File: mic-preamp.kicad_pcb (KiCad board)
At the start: 2 copper layers, 11 parts, among them J1 Conn_01x07_Female, J2 Conn_01x04_Female, U1 LM358

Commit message: gg
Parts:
- moved R1 9.58 mm to (145.6, 104.9)
- moved C2 5.22 mm to (161.5, 100.2), turned to 0 degrees
- moved R3 3.97 mm to (165.1, 110.5), turned to 90 degrees
- moved R2 2.78 mm to (166.2, 110.7)
- moved U1 1.47 mm to (154.3, 103.6)
- moved C3 1.33 mm to (152.8, 114.4)
- moved R4 1.20 mm to (152.5, 100.1)
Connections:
- J1 pad 2: Net-(J1-Pad2) -> (no net)
- J1 pad 3: FREQUPDN -> (no net)
- J1 pad 4: Net-(J1-Pad4) -> (no net)
- J2 pad 2: MICOUT -> PTT
- J2 pad 3: PTT -> MICGND
- J2 pad 4: MICGND -> MICOUT
- U1 pad 1: MICOUT -> (no net)
- U1 pad 2: Net-(C3-Pad2) -> (no net)
- U1 pad 3: +2V5 -> (no net)
- U1 pad 5: (no net) -> +2V5
- U1 pad 6: (no net) -> Net-(C3-Pad2)
- U1 pad 7: (no net) -> MICOUT
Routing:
- net PTT: track 0.00 -> 56.2 mm
- net +2V5: track 3.55 -> 32.0 mm
- net MICOUT: track 53.4 -> 26.3 mm
- net +5V: track 18.2 -> 41.4 mm
- net MICIN: track 6.13 -> 21.7 mm
- net Net-(C1-Pad2): track 5.51 -> 6.72 mm
- net Net-(C3-Pad2): track 19.3 -> 18.4 mm
- net MICGND: vias 0 -> 2
- added copper zone on B.Cu, net MICGND
- added copper zone on F.Cu, net MICGND
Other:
- board outline added: 42.5 x 23.7 mm

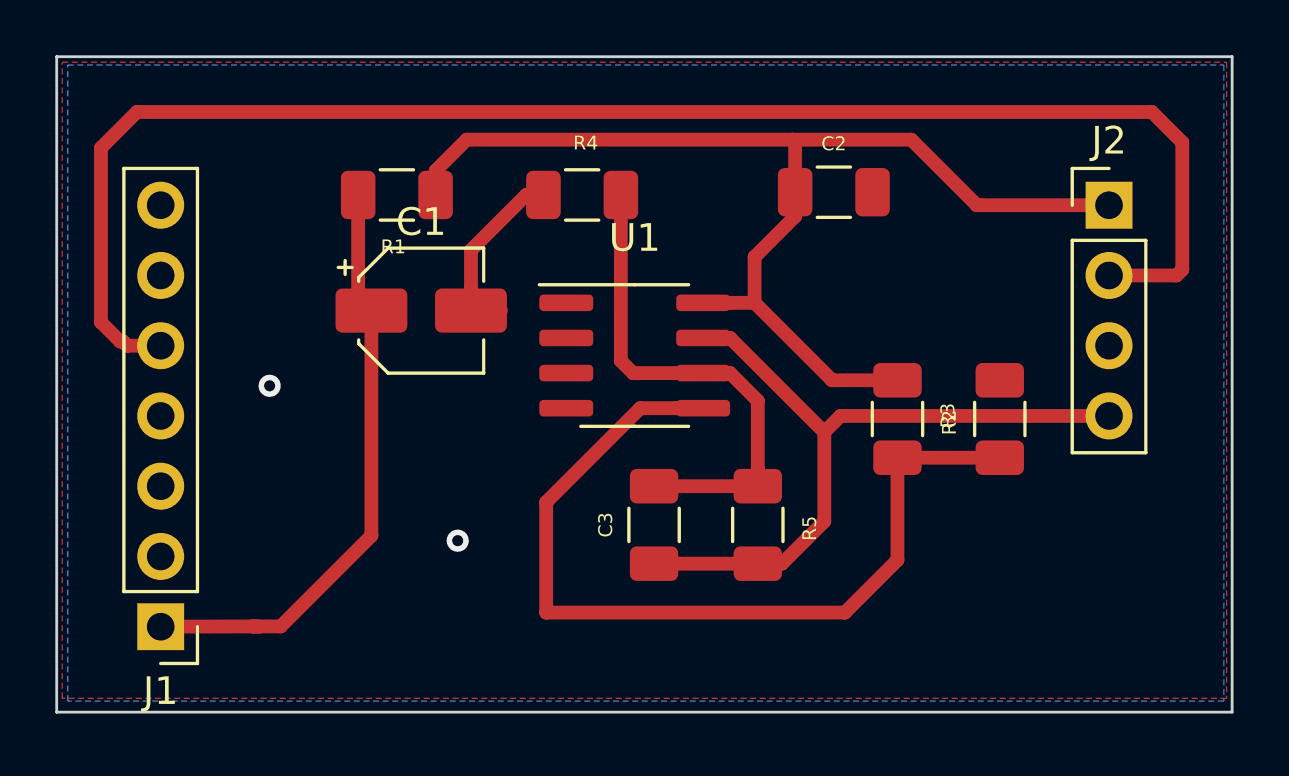
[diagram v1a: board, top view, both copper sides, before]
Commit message: added output cap
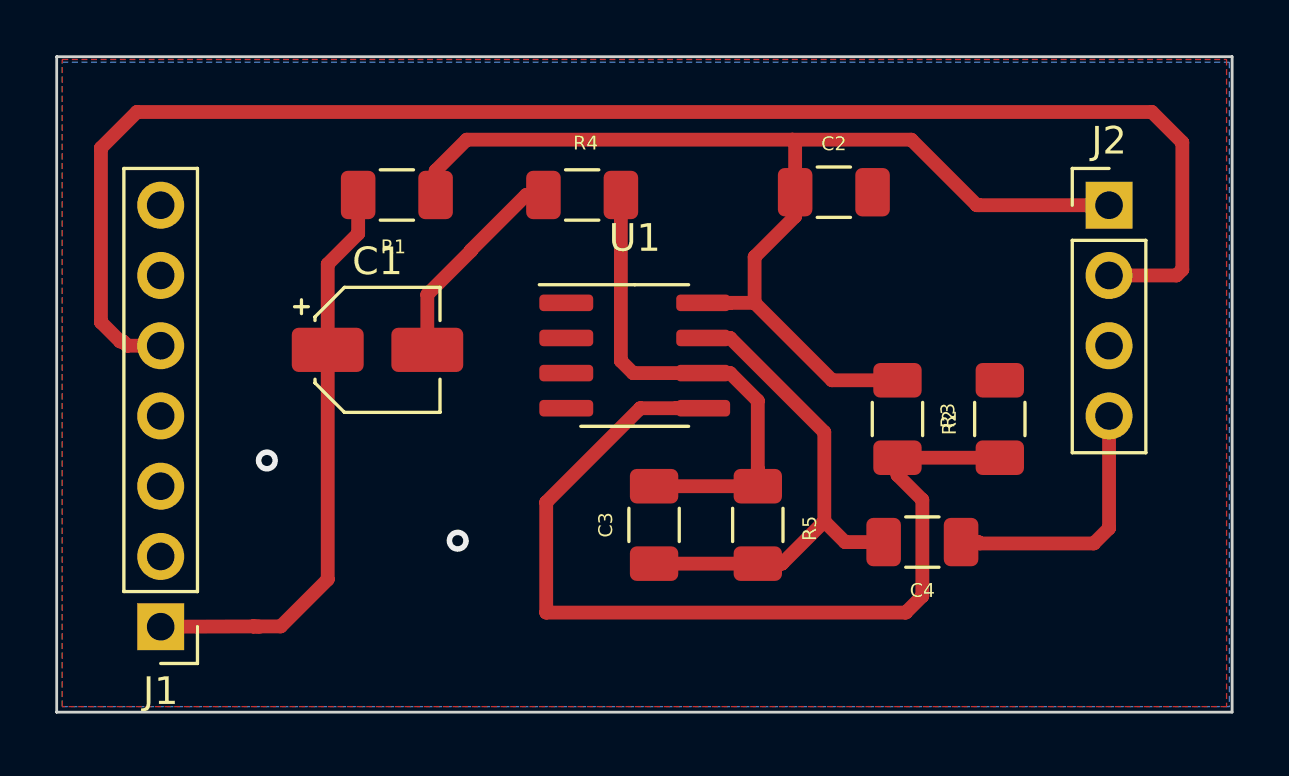
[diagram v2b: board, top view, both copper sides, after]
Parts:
- added C4: 100nF, Xenir:Capacitor 1206, F.Cu at (164.7, 117.3)
- moved C1 2.12 mm to (145.0, 108.1)
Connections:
- C3 pad 1: MICOUT -> Net-(C3-Pad1)
- R5 pad 2: MICOUT -> Net-(C3-Pad1)
- U1 pad 7: MICOUT -> Net-(C3-Pad1)
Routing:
- net Net-(C3-Pad1): track 0.00 -> 18.3 mm
- net MICOUT: track 26.3 -> 9.66 mm
- net +2V5: track 32.0 -> 34.0 mm
- net Net-(C1-Pad2): track 6.72 -> 7.71 mm
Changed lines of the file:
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@@
     (thickness 1.6)
     (drawings 4)
-    (tracks 65)
+    (tracks 73)
     (zones 0)
-    (modules 11)
-    (nets 9)
+    (modules 12)
+    (nets 10)
   )
   (page A4)
@@
   (net 7 PTT)
   (net 8 +2V5)
+  (net 9 "Net-(C3-Pad1)")
   (net_class Default "This is the default net class."
     (clearance 0.2)
@@
     (add_net MICOUT)
     (add_net "Net-(C1-Pad2)")
+    (add_net "Net-(C3-Pad1)")
     (add_net "Net-(C3-Pad2)")
     (add_net PTT)
+  )
+  (module "Xenir:Capacitor 1206" (layer F.Cu)
+    (at 164.7 117.3 180)
+    (fp_text reference C4 (at 0 0.5) (layer F.SilkS)
+      (effects (font (size 0.5 0.5) (thickness 0.125)))
+    )
+    (fp_text value 100nF (at 0.5 4) (layer F.Fab)
+      (effects (font (size 0.5 0.5) (thickness 0.125)))
+    )
+    (fp_text user %R (at 0 2.25) (layer F.Fab)
+      (effects (font (size 0.8 0.8) (thickness 0.12)))
+    )
+    (fp_line (start -1.6 3.05) (end -1.6 1.45) (layer F.Fab) (width 0.1))
+    (fp_line (start 2.28 1.13) (end 2.28 3.37) (layer F.CrtYd) (width 0.05))
+    (fp_line (start -1.6 1.45) (end 1.6 1.45) (layer F.Fab) (width 0.1))
+    (fp_line (start -2.28 3.37) (end -2.28 1.13) (layer F.CrtYd) (width 0.05))
+    (fp_line (start -0.602064 1.34) (end 0.602064 1.34) (layer F.SilkS) (width 0.12))
+    (fp_line (start -0.602064 3.16) (end 0.602064 3.16) (layer F.SilkS) (width 0.12))
+    (fp_line (start -2.28 1.13) (end 2.28 1.13) (layer F.CrtYd) (width 0.05))
+    (fp_line (start 2.28 3.37) (end -2.28 3.37) (layer F.CrtYd) (width 0.05))
+    (fp_line (start 1.6 3.05) (end -1.6 3.05) (layer F.Fab) (width 0.1))
+    (fp_line (start 1.6 1.45) (end 1.6 3.05) (layer F.Fab) (width 0.1))
+    (pad 2 smd roundrect (at 1.4 2.25 180) (size 1.25 1.75) (layers F.Cu F.Paste F.Mask) (roundrect_rratio 0.2)
+      (net 9 "Net-(C3-Pad1)"))
+    (pad 1 smd roundrect (at -1.4 2.25 180) (size 1.25 1.75) (layers F.Cu F.Paste F.Mask) (roundrect_rratio 0.2)
+      (net 6 MICOUT))
   )
   (module "Xenir:Resistor 1206" (layer F.Cu)
@@
     (pad 3 smd roundrect (at -2.475 5.385) (size 1.95 0.6) (layers F.Cu F.Paste F.Mask) (roundrect_rratio 0.25))
     (pad 7 smd roundrect (at 2.475 4.115) (size 1.95 0.6) (layers F.Cu F.Paste F.Mask) (roundrect_rratio 0.25)
-      (net 6 MICOUT))
+      (net 9 "Net-(C3-Pad1)"))
     (pad 5 smd roundrect (at 2.475 6.655) (size 1.95 0.6) (layers F.Cu F.Paste F.Mask) (roundrect_rratio 0.25)
       (net 8 +2V5))
@@
     (fp_line (start -2.407 3.497) (end -2.407 1.257) (layer F.CrtYd) (width 0.05))
     (pad 2 smd roundrect (at 1.273 2.377 270) (size 1.25 1.75) (layers F.Cu F.Paste F.Mask) (roundrect_rratio 0.2)
-      (net 6 MICOUT))
+      (net 9 "Net-(C3-Pad1)"))
     (pad 1 smd roundrect (at -1.527 2.377 270) (size 1.25 1.75) (layers F.Cu F.Paste F.Mask) (roundrect_rratio 0.2)
       (net 5 "Net-(C3-Pad2)"))
@@
       (net 5 "Net-(C3-Pad2)"))
     (pad 1 smd roundrect (at -1.4 2.25 90) (size 1.25 1.75) (layers F.Cu F.Paste F.Mask) (roundrect_rratio 0.2)
-      (net 6 MICOUT))
+      (net 9 "Net-(C3-Pad1)"))
   )
   (module "Xenir:Capacitor 1206" (layer F.Cu)
@@
   )
   (module Capacitor_SMD:CP_Elec_4x5.4 (layer F.Cu)
-    (at 146.58 106.68)
+    (at 145 108.1)
     (descr "SMD capacitor, aluminum electrolytic, Panasonic A5 / Nichicon, 4.0x5.4mm")
     (tags "capacitor electrolytic")
@@
   (gr_line (start 133.4 121.2) (end 133.4 97.5) (layer Edge.Cuts) (width 0.1))
   (gr_line (start 175.9 121.2) (end 133.4 121.2) (layer Edge.Cuts) (width 0.1))
-  (segment (start 149.465 106.68) (end 148.38 106.68) (width 0.5) (layer F.Cu) (net 1))
-  (segment (start 148.38 105.88) (end 148.38 106.68) (width 0.5) (layer F.Cu) (net 1))
+  (segment (start 146.8 106.1) (end 146.8 108.1) (width 0.5) (layer F.Cu) (net 1))
+  (segment (start 148.38 104.52) (end 146.8 106.1) (width 0.5) (layer F.Cu) (net 1))
+  (segment (start 148.38 104.495) (end 148.38 104.52) (width 0.5) (layer F.Cu) (net 1))
+  (segment (start 151 102.5) (end 150.375 102.5) (width 0.5) (layer F.Cu) (net 1))
   (segment (start 150.375 102.5) (end 148.38 104.495) (width 0.5) (layer F.Cu) (net 1))
-  (segment (start 148.38 104.495) (end 148.38 105.88) (width 0.5) (layer F.Cu) (net 1))
-  (segment (start 151 102.5) (end 150.375 102.5) (width 0.5) (layer F.Cu) (net 1))
-  (segment (start 144.3 106.2) (end 144.78 106.68) (width 0.5) (layer F.Cu) (net 2))
-  (segment (start 144.3 102.5) (end 144.3 106.2) (width 0.5) (layer F.Cu) (net 2))
-  (segment (start 144.78 106.68) (end 144.78 114.82) (width 0.5) (layer F.Cu) (net 2))
   (segment (start 141.5 118.1) (end 140.5 118.1) (width 0.5) (layer F.Cu) (net 2))
-  (segment (start 144.78 114.82) (end 141.5 118.1) (width 0.5) (layer F.Cu) (net 2))
   (segment (start 137.16 118.11) (end 140.5 118.1) (width 0.5) (layer F.Cu) (net 2))
   (segment (start 140.5 118.1) (end 140.735 118.11) (width 0.5) (layer F.Cu) (net 2))
-  (via (at 141.1 109.4) (size 0.8) (drill 0.4) (layers F.Cu B.Cu) (net 3))
+  (segment (start 144.3 102.5) (end 144.3 103.9) (width 0.5) (layer F.Cu) (net 2))
+  (segment (start 143.2 105) (end 143.2 108.1) (width 0.5) (layer F.Cu) (net 2))
+  (segment (start 144.3 103.9) (end 143.2 105) (width 0.5) (layer F.Cu) (net 2))
+  (segment (start 143.2 116.4) (end 141.5 118.1) (width 0.5) (layer F.Cu) (net 2))
+  (segment (start 143.2 108.1) (end 143.2 116.4) (width 0.5) (layer F.Cu) (net 2))
+  (via (at 141 112.1) (size 0.8) (drill 0.4) (layers F.Cu B.Cu) (net 3))
   (via (at 147.9 115) (size 0.8) (drill 0.4) (layers F.Cu B.Cu) (net 3))
   (segment (start 171.45 102.87) (end 166.755 102.87) (width 0.5) (layer F.Cu) (net 4))
@@
   (segment (start 153.8 108.5) (end 154.24 108.94) (width 0.5) (layer F.Cu) (net 5))
   (segment (start 158.75 113.03) (end 155 113.03) (width 0.5) (layer F.Cu) (net 5))
-  (segment (start 161.155 111.075) (end 161.155 114.3) (width 0.5) (layer F.Cu) (net 6))
-  (segment (start 159.625 115.83) (end 158.75 115.83) (width 0.5) (layer F.Cu) (net 6))
-  (segment (start 161.155 114.3) (end 159.625 115.83) (width 0.5) (layer F.Cu) (net 6))
-  (segment (start 157.75 107.67) (end 161.155 111.075) (width 0.5) (layer F.Cu) (net 6))
-  (segment (start 156.775 107.67) (end 157.75 107.67) (width 0.5) (layer F.Cu) (net 6))
-  (segment (start 161.74 110.49) (end 171.45 110.49) (width 0.5) (layer F.Cu) (net 6))
-  (segment (start 161.155 111.075) (end 161.74 110.49) (width 0.5) (layer F.Cu) (net 6))
-  (segment (start 158.75 115.83) (end 155 115.83) (width 0.5) (layer F.Cu) (net 6))
+  (segment (start 166.725 115.05) (end 166.775 115.1) (width 0.5) (layer F.Cu) (net 6))
+  (segment (start 166.1 115.05) (end 166.725 115.05) (width 0.5) (layer F.Cu) (net 6))
+  (segment (start 166.775 115.1) (end 170.9 115.1) (width 0.5) (layer F.Cu) (net 6))
+  (segment (start 171.45 114.55) (end 171.45 110.49) (width 0.5) (layer F.Cu) (net 6))
+  (segment (start 170.9 115.1) (end 171.45 114.55) (width 0.5) (layer F.Cu) (net 6))
+  (segment (start 161.155 111.075) (end 161.155 114.3) (width 0.5) (layer F.Cu) (net 9))
+  (segment (start 159.625 115.83) (end 158.75 115.83) (width 0.5) (layer F.Cu) (net 9))
+  (segment (start 161.155 114.3) (end 159.625 115.83) (width 0.5) (layer F.Cu) (net 9))
+  (segment (start 157.75 107.67) (end 161.155 111.075) (width 0.5) (layer F.Cu) (net 9))
+  (segment (start 156.775 107.67) (end 157.75 107.67) (width 0.5) (layer F.Cu) (net 9))
+  (segment (start 158.75 115.83) (end 155 115.83) (width 0.5) (layer F.Cu) (net 9))
   (segment (start 174.1 105.2) (end 173.89 105.41) (width 0.5) (layer F.Cu) (net 7))
   (segment (start 173 99.5) (end 174.1 100.6) (width 0.5) (layer F.Cu) (net 7))
@@
   (segment (start 135.7 107.8) (end 135 107.1) (width 0.5) (layer F.Cu) (net 7))
   (segment (start 167.5 112) (end 163.8 112) (width 0.5) (layer F.Cu) (net 8))
-  (segment (start 155.8 110.21) (end 156.775 110.21) (width 0.5) (layer F.Cu) (net 8))
-  (segment (start 163.8 112) (end 163.8 115.7) (width 0.5) (layer F.Cu) (net 8))
-  (segment (start 163.8 115.7) (end 161.9 117.6) (width 0.5) (layer F.Cu) (net 8))
   (segment (start 154.500034 110.21) (end 155.8 110.21) (width 0.5) (layer F.Cu) (net 8))
   (segment (start 151.1 117.6) (end 151.1 113.610034) (width 0.5) (layer F.Cu) (net 8))
-  (segment (start 161.9 117.6) (end 151.1 117.6) (width 0.5) (layer F.Cu) (net 8))
+  (segment (start 163.8 112.625) (end 164.7 113.525) (width 0.5) (layer F.Cu) (net 8))
+  (segment (start 163.8 112) (end 163.8 112.625) (width 0.5) (layer F.Cu) (net 8))
+  (segment (start 164.7 113.525) (end 164.7 117) (width 0.5) (layer F.Cu) (net 8))
+  (segment (start 164.7 117) (end 164.1 117.6) (width 0.5) (layer F.Cu) (net 8))
+  (segment (start 155.8 110.21) (end 156.775 110.21) (width 0.5) (layer F.Cu) (net 8))
   (segment (start 151.1 113.610034) (end 154.500034 110.21) (width 0.5) (layer F.Cu) (net 8))
+  (segment (start 164.1 117.6) (end 151.1 117.6) (width 0.5) (layer F.Cu) (net 8))
+  (segment (start 161.905 115.05) (end 163.3 115.05) (width 0.5) (layer F.Cu) (net 9))
+  (segment (start 161.155 114.3) (end 161.905 115.05) (width 0.5) (layer F.Cu) (net 9))
   (zone (net 3) (net_name MICGND) (layer F.Cu) (hatch edge 0.508)
     (connect_pads (clearance 0.508))
@@
     (polygon
       (pts
-        (xy 175.7 120.7) (xy 133.6 120.7) (xy 133.6 97.7) (xy 175.7 97.7)
+        (xy 175.7 121) (xy 133.6 121) (xy 133.6 97.6) (xy 175.7 97.6)
       )
     )
@@
     (polygon
       (pts
-        (xy 175.6 120.8) (xy 133.8 120.8) (xy 133.8 97.8) (xy 175.6 97.8)
+        (xy 175.8 121) (xy 133.6 121) (xy 133.6 97.7) (xy 175.8 97.7)
       )
     )

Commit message: 330pF
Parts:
- C3: value 330nF -> 330pF
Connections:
- J1 pad 2: (no net) -> Net-(J1-Pad2)
- J1 pad 3: (no net) -> FREQUPDN
- J1 pad 4: (no net) -> Net-(J1-Pad4)
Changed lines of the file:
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@@
-(kicad_pcb (version 20171130) (host pcbnew "(5.1.5)-3")
+(kicad_pcb (version 20171130) (host pcbnew 5.1.5+dfsg1-2build2)
   (general
     (thickness 1.6)
@@
     (zones 0)
     (modules 12)
-    (nets 10)
+    (nets 13)
   )
   (page A4)
@@
   )
   (setup
-    (last_trace_width 0.5)
+    (last_trace_width 0.25)
     (user_trace_width 0.5)
     (trace_clearance 0.2)
@@
   (net 8 +2V5)
   (net 9 "Net-(C3-Pad1)")
+  (net 10 "Net-(J1-Pad4)")
+  (net 11 FREQUPDN)
+  (net 12 "Net-(J1-Pad2)")
   (net_class Default "This is the default net class."
     (clearance 0.2)
@@
     (add_net +2V5)
     (add_net +5V)
+    (add_net FREQUPDN)
     (add_net MICGND)
     (add_net MICIN)
@@
     (add_net "Net-(C3-Pad1)")
     (add_net "Net-(C3-Pad2)")
+    (add_net "Net-(J1-Pad2)")
+    (add_net "Net-(J1-Pad4)")
     (add_net PTT)
   )
@@
     (pad 5 thru_hole oval (at 0 10.16 180) (size 1.7 1.7) (drill 1) (layers *.Cu *.Mask)
       (net 7 PTT))
-    (pad 4 thru_hole oval (at 0 7.62 180) (size 1.7 1.7) (drill 1) (layers *.Cu *.Mask))
-    (pad 3 thru_hole oval (at 0 5.08 180) (size 1.7 1.7) (drill 1) (layers *.Cu *.Mask))
-    (pad 2 thru_hole oval (at 0 2.54 180) (size 1.7 1.7) (drill 1) (layers *.Cu *.Mask))
+    (pad 4 thru_hole oval (at 0 7.62 180) (size 1.7 1.7) (drill 1) (layers *.Cu *.Mask)
+      (net 10 "Net-(J1-Pad4)"))
+    (pad 3 thru_hole oval (at 0 5.08 180) (size 1.7 1.7) (drill 1) (layers *.Cu *.Mask)
+      (net 11 FREQUPDN))
+    (pad 2 thru_hole oval (at 0 2.54 180) (size 1.7 1.7) (drill 1) (layers *.Cu *.Mask)
+      (net 12 "Net-(J1-Pad2)"))
     (pad 1 thru_hole rect (at 0 0 180) (size 1.7 1.7) (drill 1) (layers *.Cu *.Mask)
       (net 2 MICIN))
@@
       (effects (font (size 0.5 0.5) (thickness 0.125)))
     )
-    (fp_text value 330nF (at 0.5 4 90) (layer F.Fab)
+    (fp_text value 330pF (at 0.5 4 90) (layer F.Fab)
       (effects (font (size 0.5 0.5) (thickness 0.125)))
     )
@@
   (segment (start 171.45 114.55) (end 171.45 110.49) (width 0.5) (layer F.Cu) (net 6))
   (segment (start 170.9 115.1) (end 171.45 114.55) (width 0.5) (layer F.Cu) (net 6))
-  (segment (start 161.155 111.075) (end 161.155 114.3) (width 0.5) (layer F.Cu) (net 9))
-  (segment (start 159.625 115.83) (end 158.75 115.83) (width 0.5) (layer F.Cu) (net 9))
-  (segment (start 161.155 114.3) (end 159.625 115.83) (width 0.5) (layer F.Cu) (net 9))
-  (segment (start 157.75 107.67) (end 161.155 111.075) (width 0.5) (layer F.Cu) (net 9))
-  (segment (start 156.775 107.67) (end 157.75 107.67) (width 0.5) (layer F.Cu) (net 9))
-  (segment (start 158.75 115.83) (end 155 115.83) (width 0.5) (layer F.Cu) (net 9))
   (segment (start 174.1 105.2) (end 173.89 105.41) (width 0.5) (layer F.Cu) (net 7))
   (segment (start 173 99.5) (end 174.1 100.6) (width 0.5) (layer F.Cu) (net 7))
@@
   (segment (start 151.1 113.610034) (end 154.500034 110.21) (width 0.5) (layer F.Cu) (net 8))
   (segment (start 164.1 117.6) (end 151.1 117.6) (width 0.5) (layer F.Cu) (net 8))
+  (segment (start 161.155 111.075) (end 161.155 114.3) (width 0.5) (layer F.Cu) (net 9))
+  (segment (start 159.625 115.83) (end 158.75 115.83) (width 0.5) (layer F.Cu) (net 9))
+  (segment (start 161.155 114.3) (end 159.625 115.83) (width 0.5) (layer F.Cu) (net 9))
+  (segment (start 157.75 107.67) (end 161.155 111.075) (width 0.5) (layer F.Cu) (net 9))
+  (segment (start 156.775 107.67) (end 157.75 107.67) (width 0.5) (layer F.Cu) (net 9))
+  (segment (start 158.75 115.83) (end 155 115.83) (width 0.5) (layer F.Cu) (net 9))
   (segment (start 161.905 115.05) (end 163.3 115.05) (width 0.5) (layer F.Cu) (net 9))
   (segment (start 161.155 114.3) (end 161.905 115.05) (width 0.5) (layer F.Cu) (net 9))
